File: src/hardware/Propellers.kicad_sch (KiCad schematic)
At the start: 17 parts, among them J201 CPU PGMR, J202 SPARE CPU HDR, J203 GPU PGMR, J204 SPARE GPU HDR, SW201 CPU ~{RES}, SW202 DEBUG, SW203 GPU ~{RES}

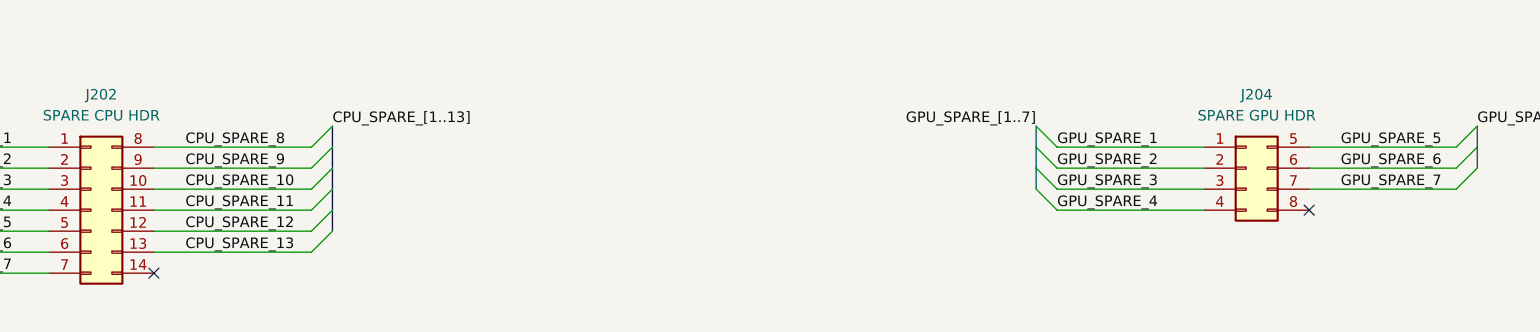
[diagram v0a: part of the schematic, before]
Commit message: Added GND pins to spare headers
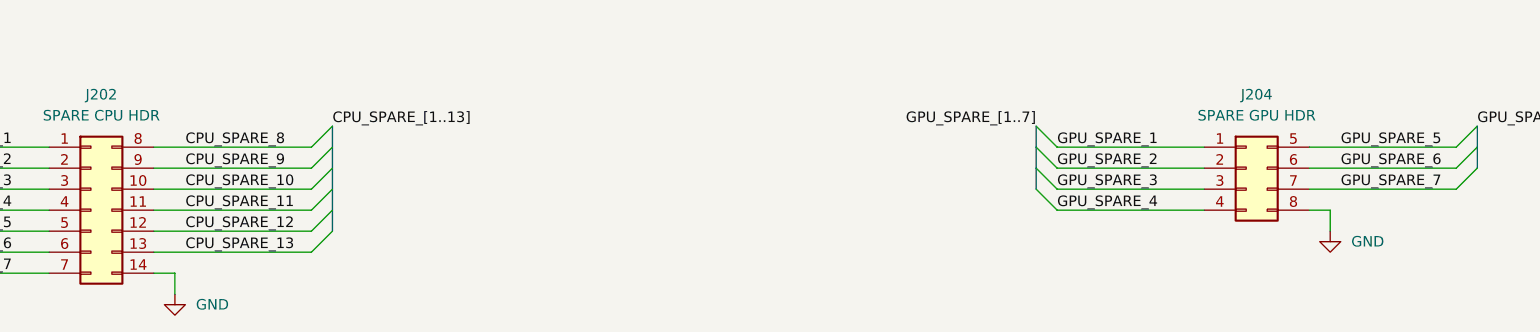
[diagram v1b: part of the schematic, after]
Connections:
- net GND: now also J202.14 (Pin_14), J204.8 (Pin_8)
- no-connect marks 6 -> 4
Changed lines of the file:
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@@
   (junction (at 67.31 57.15) (diameter 0) (color 0 0 0 0)
   )
-  (no_connect (at 222.25 158.75))
-  (no_connect (at 82.55 166.37))
   (no_connect (at 92.71 99.06))
   (no_connect (at 232.41 106.68))
@@
     (stroke (width 0) (type default))
   )
+  (wire (pts (xy 85.09 166.37) (xy 85.09 168.91))
+    (stroke (width 0) (type default))
+  )
   (wire (pts (xy 92.71 93.98) (xy 120.65 93.98))
     (stroke (width 0) (type default))
@@
     (stroke (width 0) (type default))
   )
+  (wire (pts (xy 82.55 166.37) (xy 85.09 166.37))
+    (stroke (width 0) (type default))
+  )
   (bus (pts (xy 123.19 78.74) (xy 123.19 76.2))
     (stroke (width 0) (type default))
@@
     (stroke (width 0) (type default))
   )
+  (wire (pts (xy 224.79 158.75) (xy 224.79 161.29))
+    (stroke (width 0) (type default))
+  )
   (wire (pts (xy 158.75 33.02) (xy 154.94 33.02))
     (stroke (width 0) (type default))
@@
   )
   (wire (pts (xy 36.83 63.5) (xy 40.64 63.5))
+    (stroke (width 0) (type default))
+  )
+  (wire (pts (xy 222.25 158.75) (xy 224.79 158.75))
     (stroke (width 0) (type default))
   )
@@
         )
       )
+    )
+  )
+  (symbol (lib_id "power:GND") (at 224.79 161.29 0) (unit 1)
+    (in_bom yes) (on_board yes) (dnp no) (fields_autoplaced)
+    (property "Reference" "#PWR0220" (at 224.79 167.64 0)
+      (effects (font (size 1.27 1.27)) hide)
+    )
+    (property "Value" "GND" (at 227.33 162.56 0)
+      (effects (font (size 1.27 1.27)) (justify left))
+    )
+    (property "Footprint" "" (at 224.79 161.29 0)
+      (effects (font (size 1.27 1.27)) hide)
+    )
+    (property "Datasheet" "" (at 224.79 161.29 0)
+      (effects (font (size 1.27 1.27)) hide)
+    )
+    (pin "1")
+    (instances
+      (project "jcap"
+        (path "/7fc25e9e-3600-419b-89ef-b962e4e374c1/203ea849-2dbb-4e64-89c6-7fa05a05e11f"
+          (reference "#PWR0220") (unit 1)
+        )
+      )
+    )
+  )
+  (symbol (lib_id "power:GND") (at 85.09 168.91 0) (unit 1)
+    (in_bom yes) (on_board yes) (dnp no) (fields_autoplaced)
+    (property "Reference" "#PWR0219" (at 85.09 175.26 0)
+      (effects (font (size 1.27 1.27)) hide)
+    )
+    (property "Value" "GND" (at 87.63 170.18 0)
+      (effects (font (size 1.27 1.27)) (justify left))
+    )
+    (property "Footprint" "" (at 85.09 168.91 0)
+      (effects (font (size 1.27 1.27)) hide)
+    )
+    (property "Datasheet" "" (at 85.09 168.91 0)
+      (effects (font (size 1.27 1.27)) hide)
+    )
+    (pin "1")
+    (instances
+      (project "jcap"
+        (path "/7fc25e9e-3600-419b-89ef-b962e4e374c1/203ea849-2dbb-4e64-89c6-7fa05a05e11f"
+          (reference "#PWR0219") (unit 1)
+        )
+      )

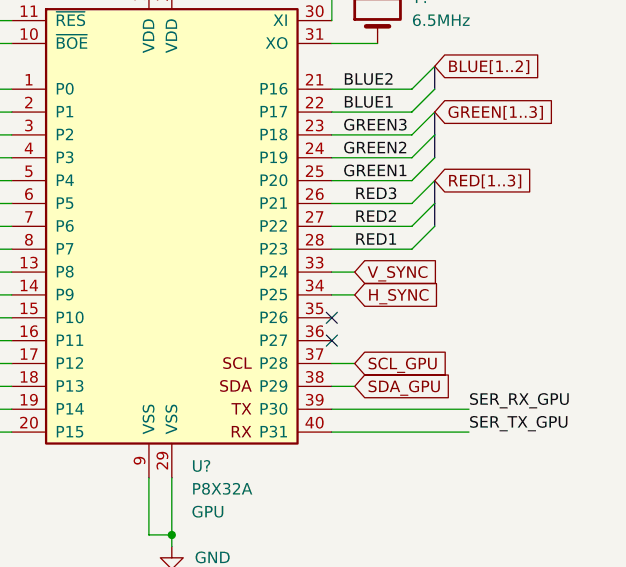
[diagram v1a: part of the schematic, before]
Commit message: Swapped H/VSync pins
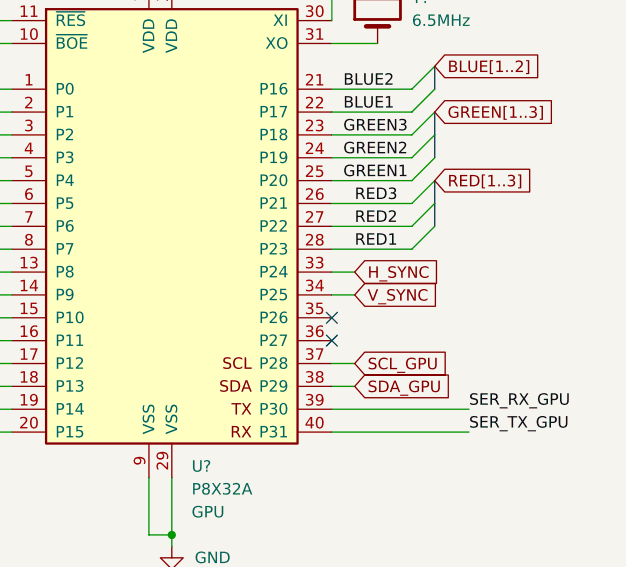
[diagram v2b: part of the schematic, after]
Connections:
- net H_SYNC: now also U?.33 (P24); no longer U?.34 (P25)
- net V_SYNC: now also U?.34 (P25); no longer U?.33 (P24)
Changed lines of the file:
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@@
     (effects (font (size 1.27 1.27)) (justify left bottom))
-  )
-  (global_label "V_SYNC" (shape input) (at 234.95 99.06 0) (fields_autoplaced)
-    (effects (font (size 1.27 1.27)) (justify left))
-    (property "Intersheetrefs" "${INTERSHEET_REFS}" (at 244.89 99.06 0)
-      (effects (font (size 1.27 1.27)) (justify left) hide)
-    )
   )
   (global_label "GREEN[1..3]" (shape input) (at 243.84 81.28 0) (fields_autoplaced)
@@
     )
   )
-  (global_label "H_SYNC" (shape input) (at 234.95 101.6 0) (fields_autoplaced)
+  (global_label "V_SYNC" (shape input) (at 234.95 101.6 0) (fields_autoplaced)
     (effects (font (size 1.27 1.27)) (justify left))
-    (property "Intersheetrefs" "${INTERSHEET_REFS}" (at 245.1319 101.6 0)
+    (property "Intersheetrefs" "${INTERSHEET_REFS}" (at 244.89 101.6 0)
       (effects (font (size 1.27 1.27)) (justify left) hide)
     )
+  )
+  (global_label "H_SYNC" (shape input) (at 234.95 99.06 0) (fields_autoplaced)
+    (effects (font (size 1.27 1.27)) (justify left))
+    (property "Intersheetrefs" "${INTERSHEET_REFS}" (at 245.1319 99.06 0)
+      (effects (font (size 1.27 1.27)) (justify left) hide)
+    )
